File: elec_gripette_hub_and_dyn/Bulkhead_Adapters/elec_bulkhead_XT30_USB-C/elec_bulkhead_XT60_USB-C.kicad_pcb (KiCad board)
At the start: 4 copper layers, 26 x 38.3 mm, 19 parts, among them J1 USB-C Rec. Vert., J2 JST EH 2, J3 XT30, J4 pico4, J5 Dynamixel-3, J6 USB_C_Receptacle, J8 USB3_A, J9 Dynamixel-3

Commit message: [update] Gripette Bulkhead DNP Dyn c.
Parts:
- J5, J9: value Dynamixel-3 -> DNP - Dynamixel-3
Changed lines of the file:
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@@
 			)
 		)
-		(property "Value" "Dynamixel-3"
+		(property "Value" "DNP - Dynamixel-3"
 			(at 2.5 3.4 0)
 			(layer "F.Fab")
@@
 		(sheetname "/")
 		(sheetfile "elec_bulkhead_XT60_USB-C.kicad_sch")
-		(attr through_hole)
+		(attr through_hole dnp)
 		(fp_line
 			(start 7.61 0.81)
@@
 			)
 		)
-		(property "Value" "Dynamixel-3"
+		(property "Value" "DNP - Dynamixel-3"
 			(at 2.5 -2.7 90)
 			(layer "B.Fab")
@@
 		(sheetname "/")
 		(sheetfile "elec_bulkhead_XT60_USB-C.kicad_sch")
-		(attr through_hole)
+		(attr through_hole dnp)
 		(fp_line
 			(start -2.61 6.81)

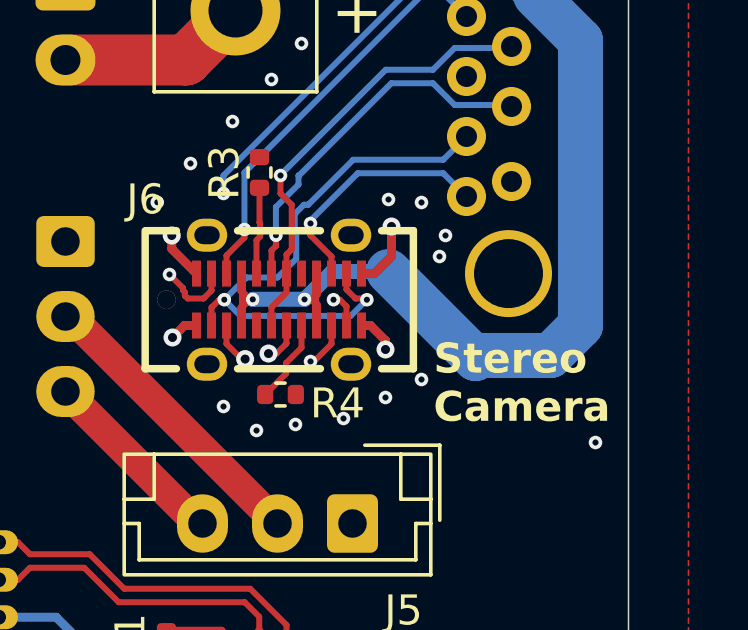
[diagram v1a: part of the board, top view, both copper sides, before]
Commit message: [fix] Bulkhead -> B2 because of a USB-C/3 extra locator pin
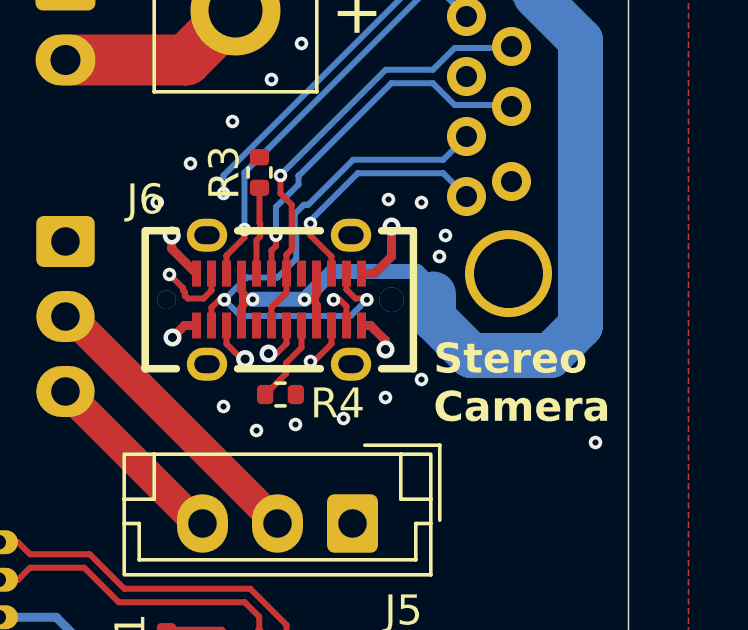
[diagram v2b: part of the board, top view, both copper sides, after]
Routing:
- net Net-(J8-VBUS): track 34.4 -> 34.9 mm
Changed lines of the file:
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@@
 	(title_block
 		(title "Grippette - Bulkhead XT30 - USB-C")
-		(date "2026-06-01")
-		(rev "B1")
+		(date "2026-07-16")
+		(rev "B2")
 		(company "Pollen Robotics / Hugging Face")
 	)
@@
 			(remove_unused_layers no)
 		)
+		(pad "" thru_hole circle
+			(at 3.75 0)
+			(size 0.82 0.82)
+			(drill 0.82)
+			(layers "*.Cu" "*.Mask")
+			(remove_unused_layers no)
+		)
 		(pad "1" thru_hole oval
 			(at 2.4 -2.15)
@@
 	)
 	(segment
-		(start 100.097501 65.140001)
-		(end 99.997501 65.240001)
-		(width 1.5)
+		(start 98.597501 62.890001)
+		(end 98.047501 62.340001)
+		(width 0.5)
 		(layer "B.Cu")
 		(net 13)
@@
 	(segment
 		(start 103.497501 64.140001)
-		(end 102.497501 65.140001)
+		(end 103.497501 54.640001)
 		(width 1.5)
 		(layer "B.Cu")
@@
 	)
 	(segment
-		(start 95.227503 62.340001)
-		(end 97.097501 62.340001)
-		(width 0.5)
+		(start 103.497501 54.640001)
+		(end 101.997501 53.140001)
+		(width 1.5)
 		(layer "B.Cu")
 		(net 13)
 	)
 	(segment
-		(start 101.197501 52.340001)
-		(end 101.997501 53.140001)
-		(width 1.3)
+		(start 102.497501 65.140001)
+		(end 103.497501 64.140001)
+		(width 1.5)
 		(layer "B.Cu")
 		(net 13)
 	)
 	(segment
-		(start 103.497501 64.140001)
-		(end 103.497501 54.640001)
-		(width 1.5)
+		(start 98.047501 62.340001)
+		(end 95.227503 62.340001)
+		(width 0.5)
 		(layer "B.Cu")
 		(net 13)
 	)
 	(segment
-		(start 103.497501 54.640001)
+		(start 101.197501 52.340001)
 		(end 101.997501 53.140001)
+		(width 1.3)
+		(layer "B.Cu")
+		(net 13)
+	)
+	(segment
+		(start 98.597501 63.090001)
+		(end 98.597501 63.890001)
 		(width 1.5)
 		(layer "B.Cu")
@@
 	)
 	(segment
-		(start 102.497501 65.140001)
-		(end 100.097501 65.140001)
+		(start 99.847501 65.140001)
+		(end 102.497501 65.140001)
 		(width 1.5)
 		(layer "B.Cu")
@@
 	)
 	(segment
-		(start 94.297501 63.270003)
-		(end 95.227503 62.340001)
+		(start 98.597501 63.090001)
+		(end 98.597501 62.890001)
+		(width 0.5)
+		(layer "B.Cu")
+		(net 13)
+	)
+	(segment
+		(start 95.227503 62.340001)
+		(end 94.297501 63.270003)
 		(width 0.5)
 		(layer "B.Cu")
@@
 	)
 	(segment
-		(start 99.997501 65.240001)
-		(end 97.097501 62.340001)
+		(start 98.597501 63.890001)
+		(end 99.847501 65.140001)
 		(width 1.5)
 		(layer "B.Cu")
